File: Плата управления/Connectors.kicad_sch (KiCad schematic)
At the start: 10 parts, among them J1 RS485, J10 Conn_02x03_Odd_Even, J12 Power, J2 CAN2, J3 CAN1, J4 A, J5 B, J6 C, J7 RS485, J8 Conn_02x03_Odd_Even

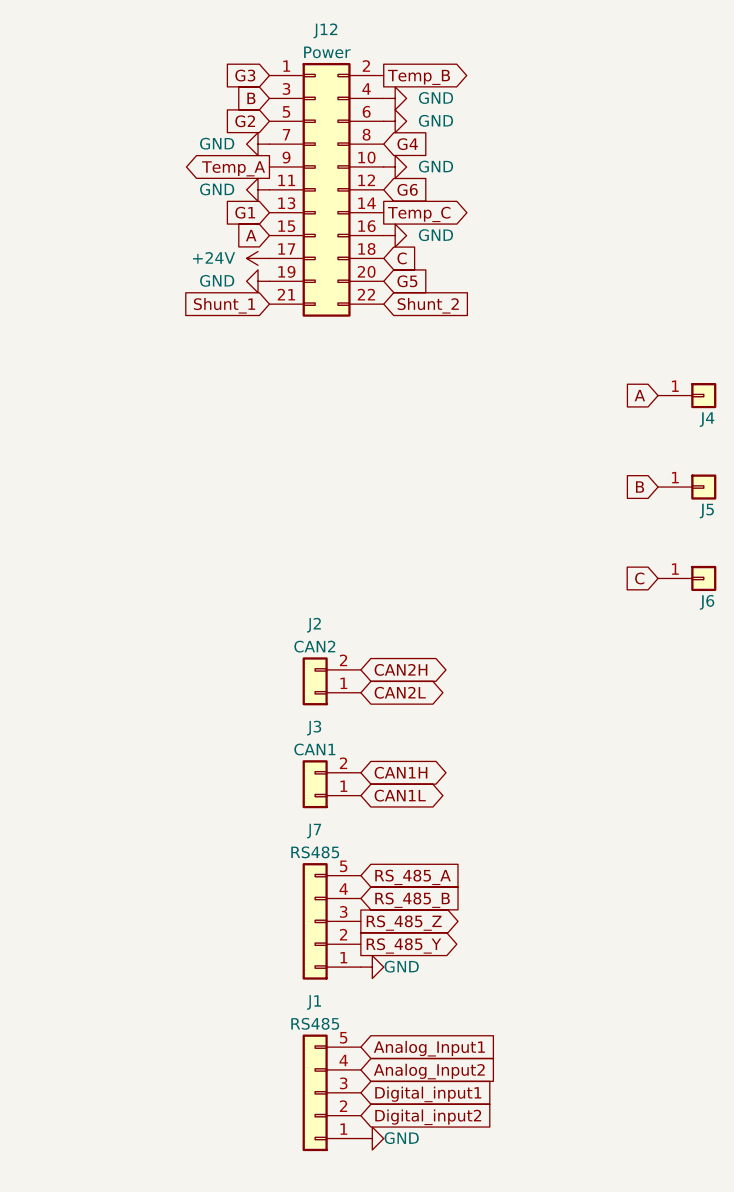
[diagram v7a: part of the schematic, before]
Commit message: Заменил разъём под силовую плату
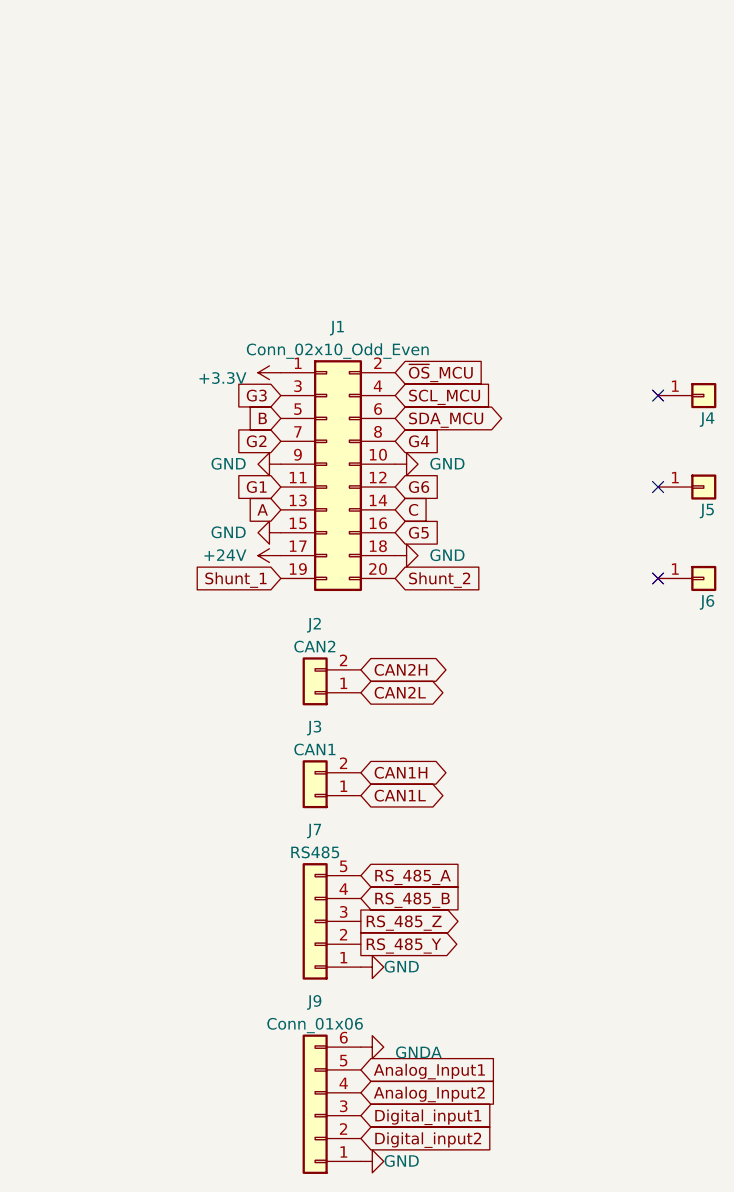
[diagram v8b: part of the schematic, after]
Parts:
- removed J1: RS485, Connector_Molex:Molex_PicoBlade_53048-0510_1x05_P1.25mm_Horizontal, symbol Connector_Generic:Conn_01x05
- removed J12: Power, Connector_PinHeader_2.54mm:PinHeader_2x11_P2.54mm_Vertical_SMD, symbol Connector_Generic:Conn_02x11_Odd_Even
- added J1: Conn_02x10_Odd_Even, Connector_PinHeader_2.54mm:PinHeader_2x10_P2.54mm_Vertical_SMD, symbol Connector_Generic:Conn_02x10_Odd_Even
- added J9: Conn_01x06, Connector_Molex:Molex_PicoBlade_53048-0610_1x06_P1.25mm_Horizontal, symbol Connector_Generic:Conn_01x06
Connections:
- net +24V: now also J1.17 (Pin_17)
- net +3.3V: now also J1.1 (Pin_1)
- net A: now also J1.13 (Pin_13); no longer J4.1 (Pin_1)
- net Analog_Input1: now also J9.5 (Pin_5)
- net Analog_Input2: now also J9.4 (Pin_4)
- net B: now also J1.5 (Pin_5); no longer J5.1 (Pin_1)
- net C: now also J1.14 (Pin_14); no longer J6.1 (Pin_1)
- net Digital_input1: now also J9.3 (Pin_3)
- net Digital_input2: now also J9.2 (Pin_2)
- net G1: now also J1.11 (Pin_11)
- net G2: now also J1.7 (Pin_7)
- net G3: now also J1.3 (Pin_3)
- net G4: now also J1.8 (Pin_8)
- net G5: now also J1.16 (Pin_16)
- net G6: now also J1.12 (Pin_12)
- net GND: now also J1.10 (Pin_10), J1.15 (Pin_15), J1.18 (Pin_18), J1.9 (Pin_9), J9.1 (Pin_1)
- net Shunt_1: now also J1.19 (Pin_19)
- net Shunt_2: now also J1.20 (Pin_20)
- new net GNDA: J9.6 (Pin_6)
- new net SCL_MCU: J1.4 (Pin_4)
- new net SDA_MCU: J1.6 (Pin_6)
- new net ~{OS}_MCU: J1.2 (Pin_2)
- no-connect marks 0 -> 3
